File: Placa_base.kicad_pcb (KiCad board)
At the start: 2 copper layers, 200 x 100 mm, 216 parts, among them J1 SWD/STLINK, J10 Interfaz con entradas digital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, J11 I2C1, J12 USART6, J13 CAN1, J14 SPI1, J15 Conn_02x08_Odd_Even, J2 Bateria, J3 Entrada 24V, J4 RS-485, J5 TV_6V, J6 AN1, J7 AN2, J8 Micro_SD_Card_Det_Hirose_DM3AT, J9 Salidas 5V, Q1 MMBT3904, Q2 MMBT3904, Q3 MMBT3904, Q4 AO3401, Q5 AO3401, SW1 SW_Push, SW2 SW_Push, SW3 SW_Push, U1 STM32F407VGTx, U10 MCP6L04T-E/ST, U11 74HCT541, U2 DC-DC_Step-Down, U3 AZ1117-3.3, U4 AZ1117-3.3, U5 RFM-0505S, U6 ISO1412, U7 WeMos_mini, U8 SIM800L_modulo, U9 Modulo_A6_Mini, Y1 32.768KHz, Y2 8MHz

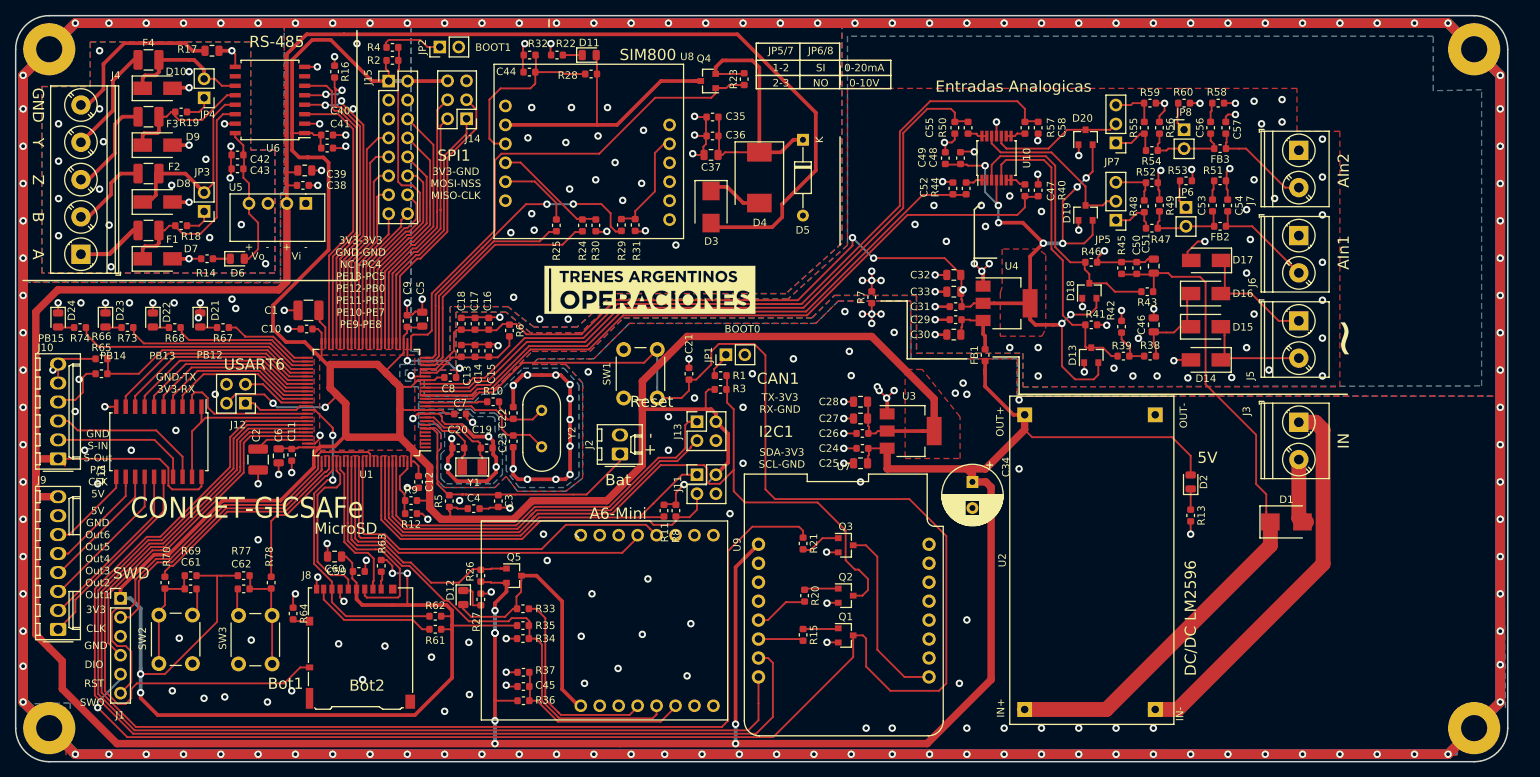
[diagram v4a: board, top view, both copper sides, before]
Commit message: Cambio de nodemcu a wemos y reducción
Se finalizó la reducción del PCB junto con el reemplazo del nodemcu por wemos d1 mini.
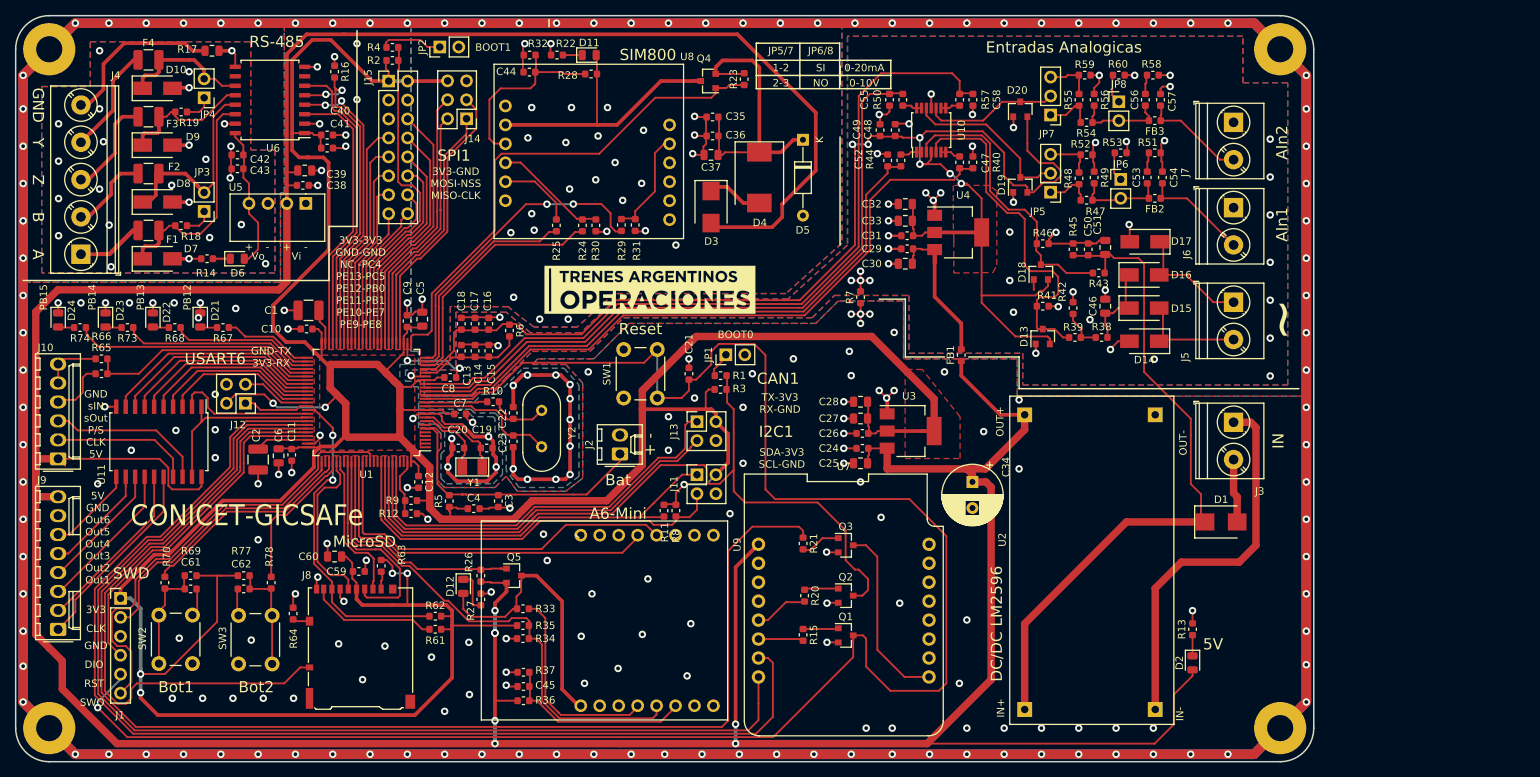
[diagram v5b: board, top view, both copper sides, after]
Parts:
- moved H2 26.0 mm to (239.5, 135.5)
- moved H3 26.0 mm to (239.5, 44.5)
- moved D2 24.3 mm to (227.8, 126.8), turned to 270 degrees
- moved R13 15.3 mm to (227.8, 122.2), turned to 90 degrees
- moved C29 11.5 mm to (189.5, 71.2)
- moved C30 11.5 mm to (189.2, 73.2)
- moved C31 11.5 mm to (189.5, 69.5)
- moved C32 11.5 mm to (189.2, 65.2)
- moved C33 11.5 mm to (189.2, 67.5)
- moved U4 11.5 mm to (196.3, 69.1)
- moved JP5 9.52 mm to (208.7, 63.7)
- moved C47 9.52 mm to (198.3, 59.7)
- moved C48 9.52 mm to (187.9, 55.3)
- moved C49 9.52 mm to (185.9, 55.3)
- moved C52 9.52 mm to (186.9, 59.4)
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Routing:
- net GND: track 1344.6 -> 1240.9 mm, vias 277 -> 261
- net +5V: track 546.7 -> 564.9 mm
- net Net-(C29-Pad1): track 9.29 -> 22.1 mm
- net VDDA: track 182.2 -> 193.7 mm, vias 12 -> 6
- net Net-(D13-Pad3): track 41.1 -> 46.9 mm
- net /analogico/AIn1: track 95.0 -> 91.1 mm
- net /An_In1: track 94.0 -> 90.3 mm
- net /An_In3: track 95.5 -> 91.8 mm
- net /An_In2: track 83.4 -> 81.1 mm
- net Net-(C46-Pad1): track 14.1 -> 12.3 mm
- net /A6_ON: track 34.1 -> 32.6 mm
- net Net-(D12-Pad2): track 35.6 -> 37.1 mm
- net Net-(D12-Pad1): track 4.19 -> 5.69 mm
- net /An_In4: track 105.8 -> 104.6 mm
- net GNDA: track 94.7 -> 93.6 mm, vias 73 -> 49
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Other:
- board size 200 x 100 mm -> 174 x 100 mm
- board text added: "GND sIN sOut P/S CLK 5V"
- board text removed: "GND S-IN S-Out P/S CLK 5V"

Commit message: PCB v1.5
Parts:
- moved G1 10.1 mm to (165.0, 75.2)
- moved C49 8.70 mm to (192.2, 61.2), turned to 270 degrees
- moved C48 8.50 mm to (194.0, 61.2), turned to 270 degrees
- moved D2 8.00 mm to (235.5, 124.8)
- moved R13 8.00 mm to (235.5, 120.2)
- moved D21 4.76 mm to (99.5, 81.0)
- moved R67 4.71 mm to (102.5, 82.0)
- moved R68 3.18 mm to (94.5, 82.0)
- moved D22 3.12 mm to (91.5, 81.0)
- moved C21 2.80 mm to (159.0, 90.5)
- moved C29 2.25 mm to (189.5, 73.5)
- moved C30 2.25 mm to (189.2, 75.5)
- moved C31 2.25 mm to (189.5, 71.8)
- moved C32 2.25 mm to (189.2, 67.5)
- moved C33 2.25 mm to (189.2, 69.8)
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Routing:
- net VDDA: track 193.7 -> 215.3 mm, vias 6 -> 4
- net /analogico/AIn1: track 91.1 -> 112.7 mm
- net GND: track 1240.9 -> 1231.3 mm
- net /NRST: track 259.9 -> 250.4 mm
- net Net-(J3-Pad1): track 51.2 -> 46.7 mm
- net GNDA: track 93.6 -> 89.3 mm, vias 49 -> 56
- net /LED1: track 12.1 -> 7.88 mm
- net /An_In4: track 104.6 -> 101.0 mm
- net Net-(R57-Pad1): track 2.78 -> 6.14 mm
- net Net-(R50-Pad1): track 2.70 -> 5.91 mm
- net Net-(R44-Pad1): track 3.02 -> 6.12 mm
- net Net-(R40-Pad1): track 2.71 -> 5.80 mm
- net /LED2: track 19.2 -> 16.2 mm
- net Net-(D13-Pad3): track 46.9 -> 44.1 mm
- net +5V: track 564.9 -> 567.3 mm
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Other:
- board size 174 x 100 mm -> 172 x 100 mm
- board text added: "(PINS)"
- board text added: "+ IN -"
- board text added: "1"
- board text added: "2"
- board text added: "3"
- board text added: "4"
- board text added: "A6-MINI"
- board text added: "B1"
- board text added: "B2"
- board text added: "BAT"
- board text added: "ENTRADAS ANALÓGICAS"
- board text added: "EXP"
- board text added: "LEDS"
- board text added: "PWR"
- board text added: "RESET"
- board text added: "WEMOS-MINI"
- board text removed: "5V"
- board text removed: "A6-Mini"
- board text removed: "Bat"
- board text removed: "Bot1"
- board text removed: "Bot2"
- board text removed: "Entradas Analogicas"
- board text removed: "IN"
- board text removed: "PB12"
- board text removed: "PB13"
- board text removed: "PB14"
- board text removed: "PB15"
- board text removed: "Reset"

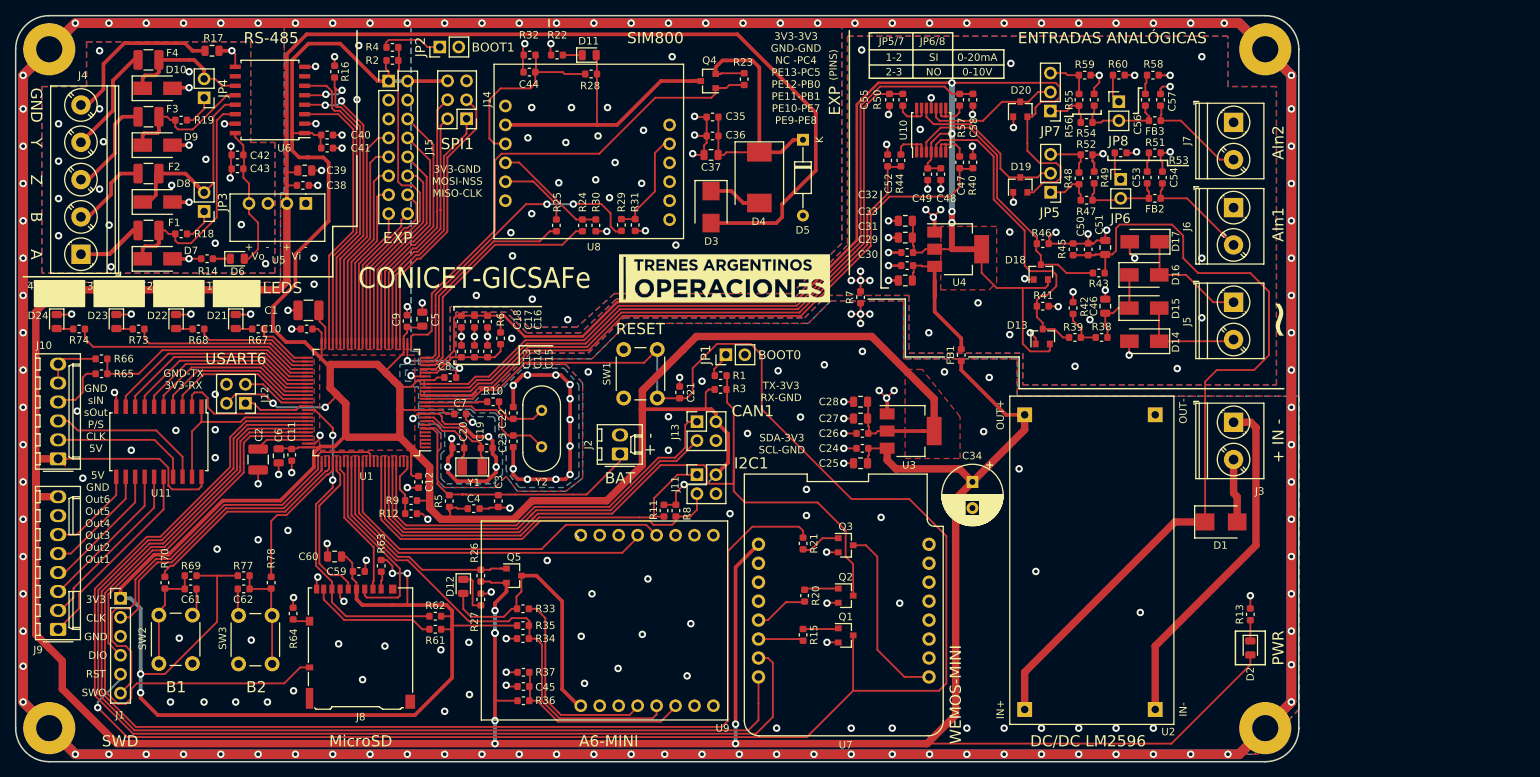
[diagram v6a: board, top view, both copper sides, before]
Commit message: PCB v1.51
Agregado de Test-point, fiduciales y modelos 3D.
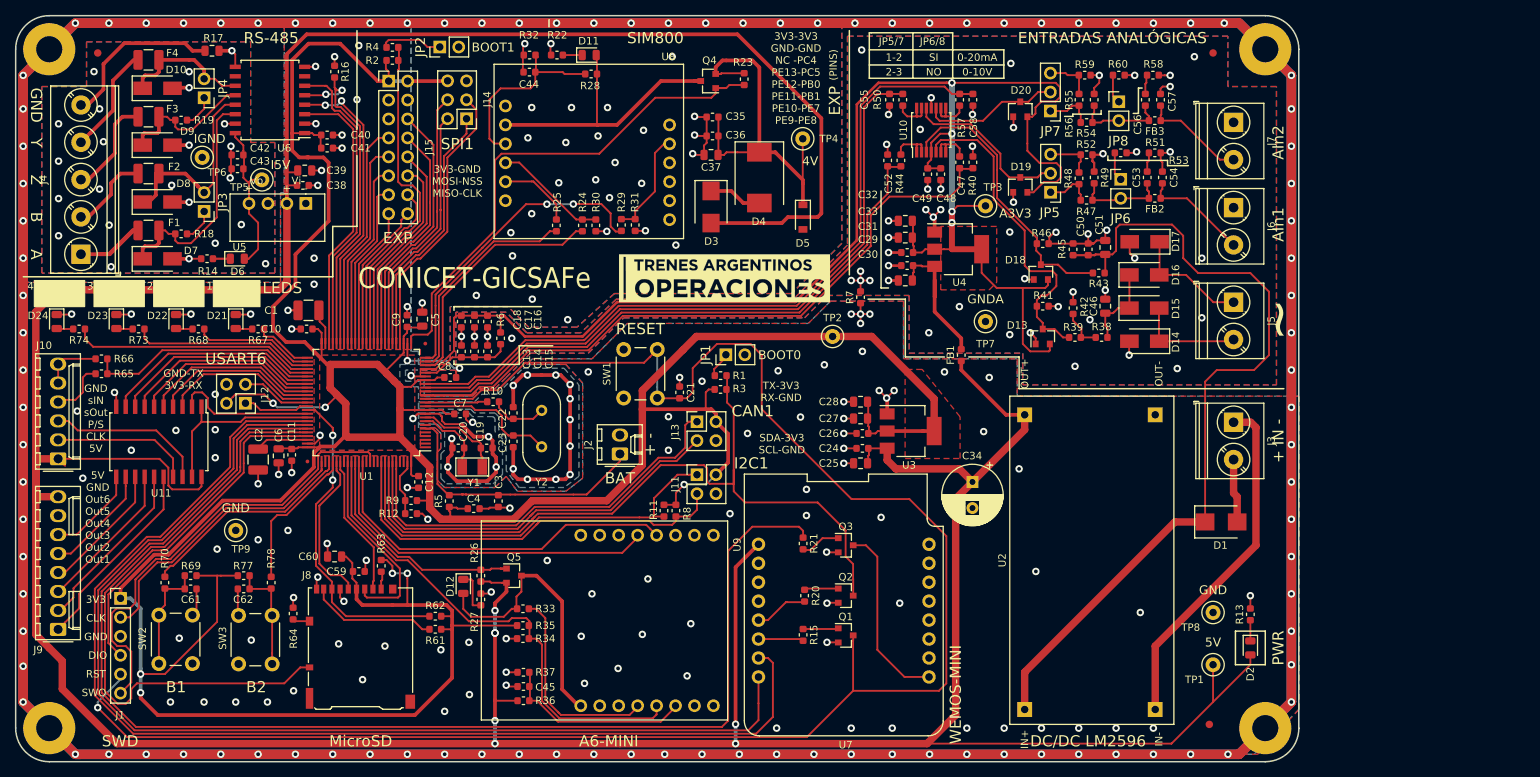
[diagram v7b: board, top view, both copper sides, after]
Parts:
- added FD1: Fiducial, Fiducial:Fiducial_1mm_Dia_2mm_Outer, F.Cu at (230.0, 135.0)
- added FD2: Fiducial, Fiducial:Fiducial_1mm_Dia_2mm_Outer, F.Cu at (230.5, 45.0)
- added FD3: Fiducial, Fiducial:Fiducial_1mm_Dia_2mm_Outer, F.Cu at (81.0, 45.0)
- added FD4: Fiducial, Fiducial:Fiducial_0.5mm_Dia_1mm_Outer, F.Cu at (109.1, 99.8)
- added FD5: Fiducial, Fiducial:Fiducial_0.5mm_Dia_1mm_Outer, F.Cu at (124.9, 84.0)
- added TP1: TestPoint, TestPoint:TestPoint_Loop_D2.50mm_Drill1.0mm, F.Cu at (230.5, 127.0)
- added TP2: TestPoint, TestPoint:TestPoint_Loop_D2.50mm_Drill1.0mm, F.Cu at (179.5, 83.0)
- added TP3: TestPoint, TestPoint:TestPoint_Loop_D2.50mm_Drill1.0mm, F.Cu at (200.0, 65.5)
- added TP4: TestPoint, TestPoint:TestPoint_Loop_D2.50mm_Drill1.0mm, F.Cu at (175.5, 56.5)
- added TP5: TestPoint, TestPoint:TestPoint_Loop_D2.50mm_Drill1.0mm, F.Cu at (103.0, 62.0)
- added TP6: TestPoint, TestPoint:TestPoint_Loop_D2.50mm_Drill1.0mm, F.Cu at (95.0, 59.0)
- added TP7: TestPoint, TestPoint:TestPoint_Loop_D2.50mm_Drill1.0mm, F.Cu at (200.0, 81.0)
- added TP8: TestPoint, TestPoint:TestPoint_Loop_D2.50mm_Drill1.0mm, F.Cu at (230.5, 120.0)
- added TP9: TestPoint, TestPoint:TestPoint_Loop_D2.50mm_Drill1.0mm, F.Cu at (99.5, 109.0)
- D5: value 1N5231CTR -> BZT52-B5V1X; footprint Diode_THT:D_DO-35_SOD27_P10.16mm_Horizontal -> Diode_SMD:D_SOD-123
- J3, J5, J6, J7: footprint TerminalBlock_Phoenix:TerminalBlock_Phoenix_PT-1,5-2-5.0-H_1x02_P5.00mm_Horizontal -> Propios:TerminalBlock_Phoenix_PT-1,5-2-5.0-H_1x02_P5.00mm_Horizontal_con_modelo3d
- J4: footprint TerminalBlock_Phoenix:TerminalBlock_Phoenix_PT-1,5-5-5.0-H_1x05_P5.00mm_Horizontal -> Propios:TerminalBlock_Phoenix_PT-1,5-5-5.0-H_1x05_P5.00mm_Horizontal_con_modelo3d
- moved D5 10.4 mm to (175.5, 67.0)
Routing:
- net +4V: track 39.8 -> 49.9 mm
- net +5V: track 567.3 -> 575.7 mm
- net VDDA: track 215.3 -> 220.2 mm
- net +5P: track 19.5 -> 21.6 mm
- net GND: track 1231.3 -> 1230.7 mm
- net Earth: vias 24 -> 22
- net (no net): vias 0 -> 1
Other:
- board text added: "4V"
- board text added: "5V"
- board text added: "A3V3"
- board text added: "GNDA"
- board text added: "I5V"
- board text added: "IGND"

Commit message: PCB 1.6. Optimizacion de 4V. Correccion de overlap entre impresiones de componentes.
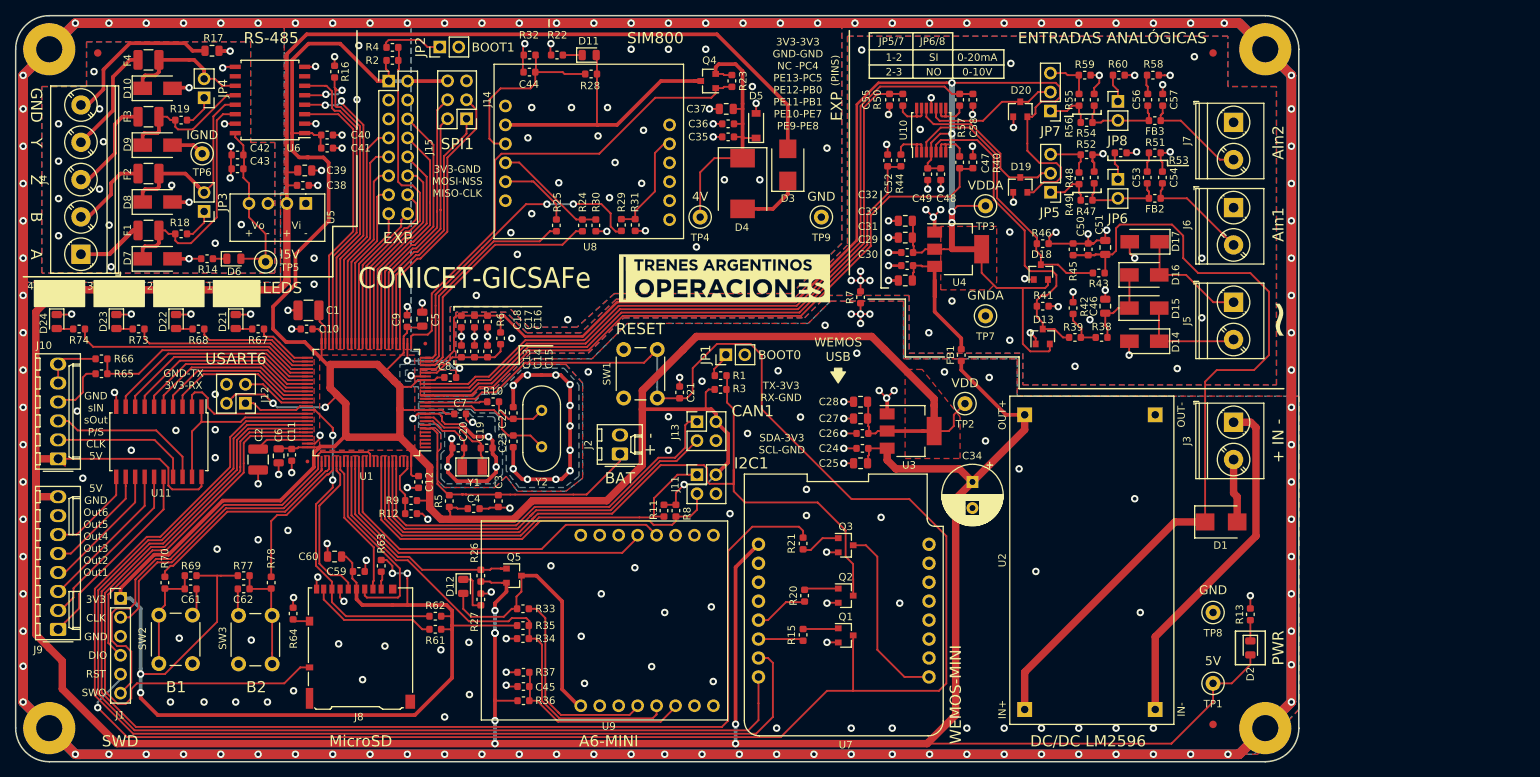
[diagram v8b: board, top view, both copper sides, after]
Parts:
- moved TP9 89.0 mm to (178.0, 67.0)
- moved TP2 19.9 mm to (197.2, 92.0)
- moved TP4 17.3 mm to (161.8, 67.0)
- moved D5 13.8 mm to (169.2, 54.8), turned to 90 degrees
- moved D3 11.7 mm to (173.5, 60.0), turned to 90 degrees
- moved TP5 11.0 mm to (103.5, 73.0)
- moved C37 6.50 mm to (165.2, 52.5)
- moved C35 3.39 mm to (165.5, 56.2)
- moved C36 2.65 mm to (165.5, 54.5)
- moved TP1 2.50 mm to (230.5, 129.5)
- moved D4 2.38 mm to (167.4, 62.5)
- moved R23 1.67 mm to (166.0, 48.8)
- moved TP7 0.75 mm to (200.0, 80.2)
- moved FD1 0.50 mm to (230.5, 135.0)
- moved TP6 0.50 mm to (95.0, 58.5)
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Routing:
- net +5V: track 575.7 -> 544.4 mm
- net +4V: track 49.9 -> 36.8 mm
- net VDD: track 508.3 -> 515.8 mm
- net GND: track 1230.7 -> 1224.9 mm, vias 261 -> 266
- net /S800_ON: track 69.1 -> 66.6 mm
- net Earth: track 21.2 -> 22.6 mm, vias 22 -> 20
- net +5P: track 21.6 -> 22.8 mm
- net Net-(D3-Pad1): track 7.70 -> 8.64 mm
- net GNDA: track 89.3 -> 88.5 mm
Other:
- board text added: "VDD"
- board text added: "VDDA"
- board text added: "WEMOS USB"
- board text removed: "A3V3"
